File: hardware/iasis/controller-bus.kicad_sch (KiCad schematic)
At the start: 10 parts, among them J1131 SM04B-SRSS-TB, J1132 UART debug, U1131 TCA9548APWR

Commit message: Wire the schematic islands and side-match the RP2354 GPIOs
Each sheet now draws its circuits with wires. Labels remain at block edges
and on single-part islands: buttons, test points, decoupling and pull
resistors. The target-port page wires its hierarchical labels straight to
the child sheet pins, the ports page points its labels away from each
block, and the root sheet keeps every block clear of the title block.

The RP2354B GPIOs are reassigned so each signal leaves the package on the
side facing its destination. Update PCB from Schematic applied the 43
U1101 pad-net changes with no geometry change. Otherwise the netlist
matches the previous design, ERC keeps its 14 existing warnings and DRC
reports no parity issues.
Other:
- moved on the sheet: R1135

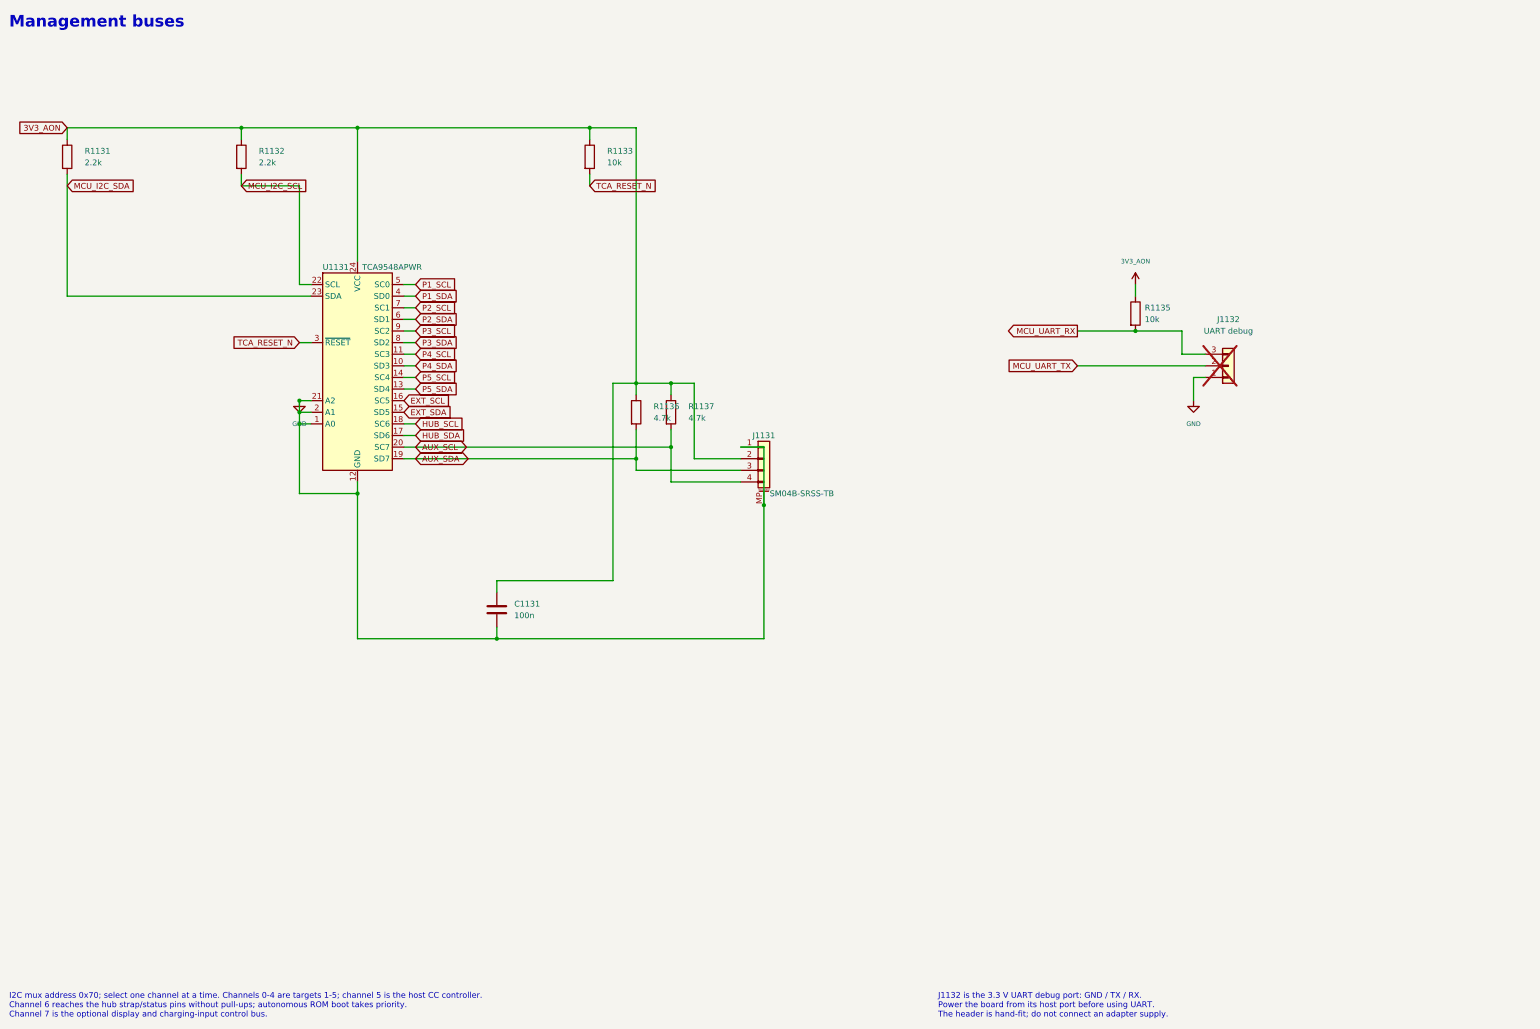
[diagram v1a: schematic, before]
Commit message: Redraw the controller support sheets
The management bus, indicator, power-control, voltage-measurement and
temperature sheets read left to right, with supplies up, ground down
and decoupling beside each IC. Pull resistors, test points and buttons
are labelled islands; everything else is wired. Supply rails use power
symbols with their existing net names, fields sit clear of bodies,
wires and text, and each sheet carries a title, date and revision. The
netlist is unchanged.
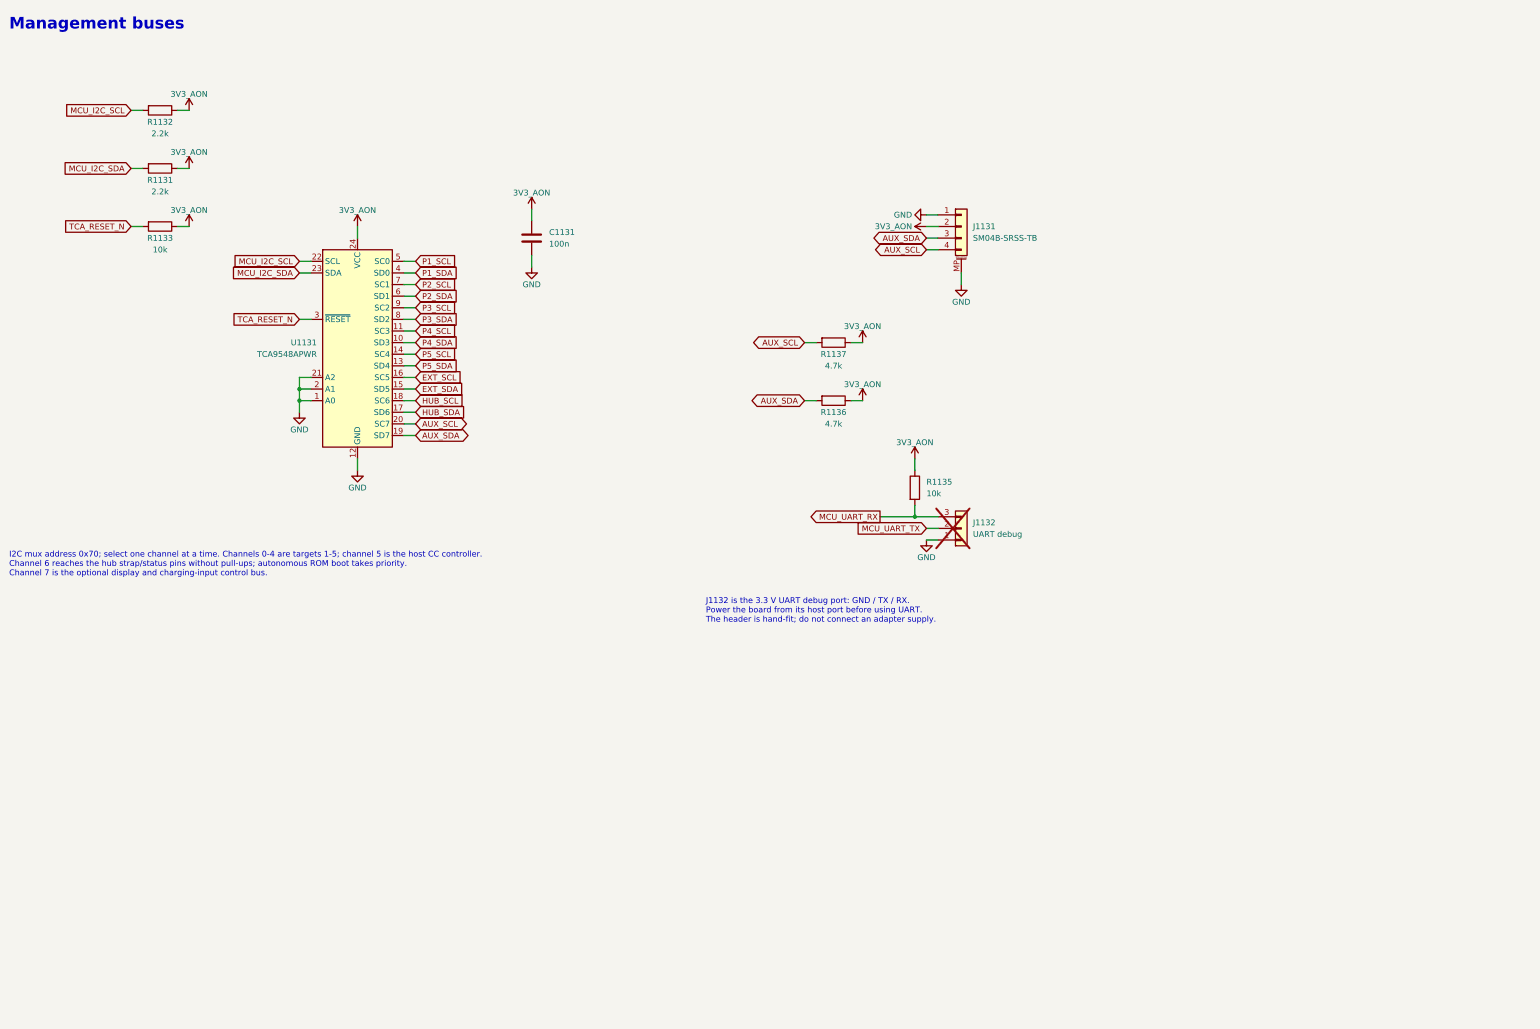
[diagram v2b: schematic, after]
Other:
- title: (none) -> Management buses
- moved on the sheet: C1131, J1131, J1132, R1131, R1132, R1133, R1135, R1136, R1137, U1131

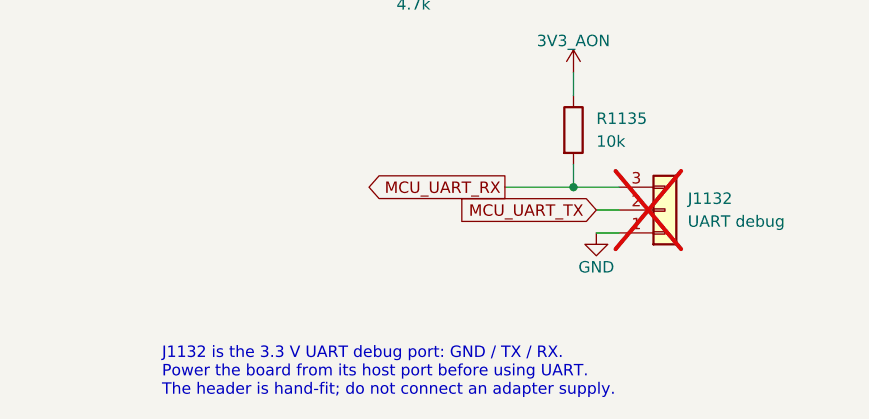
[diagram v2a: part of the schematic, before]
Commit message: Use smaller charge inductors and bulk capacitors, and solder pads for debug
The 6.8 uH PSTMAA666460 (12.5 A saturation) replaces the 10 uH 11 x 10 mm
inductor, a 6.3 mm 35 V hybrid capacitor the 10 mm 50 V bulk capacitor on
each charging buck, and an 8 mm 68 uF part the 100 uF on the charging input.
SWD and UART become three solder pads each in Raspberry Pi debug order.
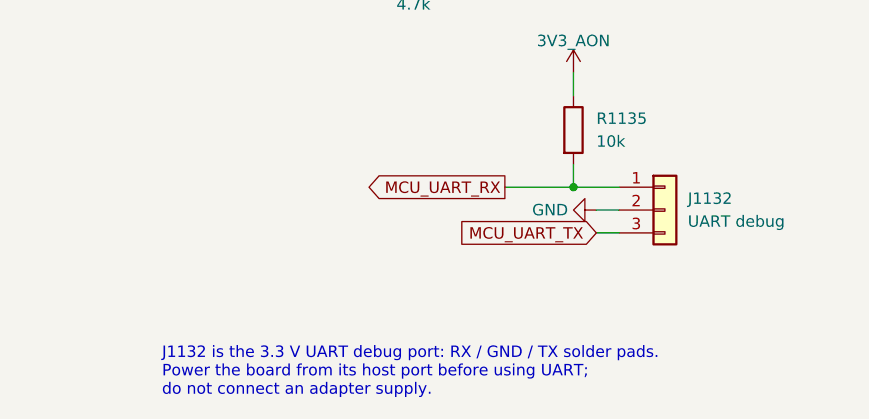
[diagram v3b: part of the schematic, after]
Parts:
- J1132: footprint Connector_PinHeader_2.54mm:PinHeader_1x03_P2.54mm_Vertical -> Iasis:SolderPads_1x03_P2.54mm; AssemblyNote Hand-fit 1x3 2.54mm header; GND / TX / RX; no adapter power -> Solder pads; RX / GND / TX; no adapter power; now fitted; now left out of the parts list
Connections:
- net GND: now also J1132.2 (Pin_2); no longer J1132.1 (Pin_1)
- net MCU_UART_RX: now also J1132.1 (Pin_1); no longer J1132.3 (Pin_3)
- net MCU_UART_TX: now also J1132.3 (Pin_3); no longer J1132.2 (Pin_2)
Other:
- note added: "J1132 is the 3.3 V UART debug port: RX / GND / TX solder pads. Power the board from its host port before using UART; do not connect an adapter supply."
- note removed: "J1132 is the 3.3 V UART debug port: GND / TX / RX. Power the board from its host port before using UART. The header is hand-fit; do not connect an adapter supply."

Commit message: fix: correct core power and recovery circuitry
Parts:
- removed R1133: 10k, Resistor_SMD:R_0402_1005Metric, symbol Device:R
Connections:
- net TCA_RESET_N renamed AON_RESET_N
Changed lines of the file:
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@@
 	(wire
 		(pts
-			(xy 54.61 66.04) (xy 52.07 66.04)
-		)
-		(stroke
-			(width 0)
-			(type default)
-		)
-	)
-	(wire
-		(pts
 			(xy 91.44 99.06) (xy 88.9 99.06)
 		)
@@
 	(wire
 		(pts
-			(xy 62.23 66.04) (xy 64.77 66.04)
-		)
-		(stroke
-			(width 0)
-			(type default)
-		)
-	)
-	(wire
-		(pts
 			(xy 209.55 104.14) (xy 212.09 104.14)
 		)
@@
 		)
 	)
-	(global_label "TCA_RESET_N"
+	(global_label "AON_RESET_N"
 		(shape input)
 		(at 88.9 86.36 180)
@@
 		)
 	)
-	(global_label "TCA_RESET_N"
-		(shape input)
-		(at 52.07 66.04 180)
-		(effects
-			(font
-				(size 1.27 1.27)
-			)
-			(justify right)
-		)
-		(property "Intersheetrefs" "${INTERSHEET_REFS}"
-			(at 52.07 66.04 0)
-			(hide yes)
-			(show_name no)
-			(do_not_autoplace no)
-			(effects
-				(font
-					(size 1.27 1.27)
-				)
-			)
-		)
-	)
 	(global_label "HUB_SDA"
 		(shape input)
@@
 	)
 	(symbol
-		(lib_id "power:+3V3")
-		(at 64.77 66.04 0)
-		(unit 1)
-		(body_style 1)
-		(exclude_from_sim no)
-		(in_bom yes)
-		(on_board yes)
-		(in_pos_files yes)
-		(dnp no)
-		(property "Reference" "#PWR5329008"
-			(at 64.77 66.04 0)
-			(hide yes)
-			(show_name no)
-			(do_not_autoplace no)
-			(effects
-				(font
-					(size 1.27 1.27)
-				)
-			)
-		)
-		(property "Value" "3V3_AON"
-			(at 64.77 62.484 0)
-			(show_name no)
-			(do_not_autoplace no)
-			(effects
-				(font
-					(size 1.27 1.27)
-				)
-			)
-		)
-		(property "Footprint" ""
-			(at 64.77 66.04 0)
-			(hide yes)
-			(show_name no)
-			(do_not_autoplace no)
-			(effects
-				(font
-					(size 1.27 1.27)
-				)
-			)
-		)
-		(property "Datasheet" ""
-			(at 64.77 66.04 0)
-			(hide yes)
-			(show_name no)
-			(do_not_autoplace no)
-			(effects
-				(font
-					(size 1.27 1.27)
-				)
-			)
-		)
-		(property "Description" ""
-			(at 64.77 66.04 0)
-			(show_name no)
-			(do_not_autoplace no)
-			(effects
-				(font
-					(size 1.27 1.27)
-				)
-			)
-		)
-		(pin "1"
-		)
-		(instances
-			(project "iasis"
-				(path "/a379403c-5d83-493f-982e-fb5e1b803ee5/fb92c4c8-3914-4e35-9e8f-8fb1a9a5c34d"
-					(reference "#PWR5329008")
-					(unit 1)
-				)
-			)
-		)
-	)
-	(symbol
 		(lib_id "Device:R")
 		(at 58.42 53.34 270)
@@
 					(unit 1)
 				)
-			)
-		)
-	)
-	(symbol
-		(lib_id "Device:R")
-		(at 58.42 66.04 270)
-		(unit 1)
-		(body_style 1)
-		(exclude_from_sim no)
-		(in_bom yes)
-		(on_board yes)
-		(in_pos_files yes)
-		(dnp no)
-		(property "Reference" "R1133"
-			(at 58.42 68.58 90)
-			(show_name no)
-			(do_not_autoplace no)
-			(effects
-				(font
-					(size 1.27 1.27)
-				)
-			)
-		)
-		(property "Value" "10k"
-			(at 58.42 71.12 90)
-			(show_name no)
-			(do_not_autoplace no)
-			(effects
-				(font
-					(size 1.27 1.27)
-				)
-			)
-		)
-		(property "Footprint" "Resistor_SMD:R_0402_1005Metric"
-			(at 58.42 66.04 0)
-			(hide yes)
-			(show_name no)
-			(do_not_autoplace no)
-			(effects
-				(font
-					(size 1.27 1.27)
-				)
-			)
-		)
-		(property "Datasheet" "https://www.lcsc.com/datasheet/lcsc_datasheet_2411221126_UNI-ROYAL-Uniroyal-Elec-0402WGF1002TCE_C25744.pdf"
-			(at 58.42 66.04 0)
-			(hide yes)
-			(show_name no)
-			(do_not_autoplace no)
-			(effects
-				(font
-					(size 1.27 1.27)
-				)
-			)
-		)
-		(property "Description" "Resistor"
-			(at 58.42 66.04 0)
-			(hide yes)
-			(show_name no)
-			(do_not_autoplace no)
-			(effects
-				(font
-					(size 1.27 1.27)
-				)
-			)
-		)
-		(property "LCSC" "C25744"
-			(at 58.42 66.04 0)
-			(hide yes)
-			(show_name no)
-			(do_not_autoplace no)
-			(effects
-				(font
-					(size 1.27 1.27)
-				)
-			)
-		)
-		(property "MPN" "0402WGF1002TCE"
-			(at 58.42 66.04 0)
-			(hide yes)
-			(show_name no)
-			(do_not_autoplace no)
-			(effects
-				(font
-					(size 1.27 1.27)
-				)
-			)
-		)
-		(property "Manufacturer" "UNI-ROYAL(Uniroyal Elec)"
-			(at 58.42 66.04 0)
-			(hide yes)
-			(show_name no)
-			(do_not_autoplace no)
-			(effects
-				(font
-					(size 1.27 1.27)
-				)
-			)
-		)
-		(pin "1"
-		)
-		(pin "2"
-		)
-		(instances
-			(project "iasis"
-				(path "/a379403c-5d83-493f-982e-fb5e1b803ee5/fb92c4c8-3914-4e35-9e8f-8fb1a9a5c34d"
-					(reference "R1133")
-					(unit 1)
-				)
